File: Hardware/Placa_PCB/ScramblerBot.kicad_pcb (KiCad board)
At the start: 4 copper layers, 79.5 x 70 mm, 74 parts, among them J1 OUT LCD, J10 Conn_01x09_Pin, J2 USB_C_Receptacle_PowerOnly_6P, J3 USB_C_Receptacle_USB2.0_16P, J4 Conn_01x03_Pin, J5 Conn_01x03_Pin, J6 Conn_01x03_Pin, J7 Conn_01x03_Pin, J8 Conn_01x08_Pin, J9 Conn_01x09_Pin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

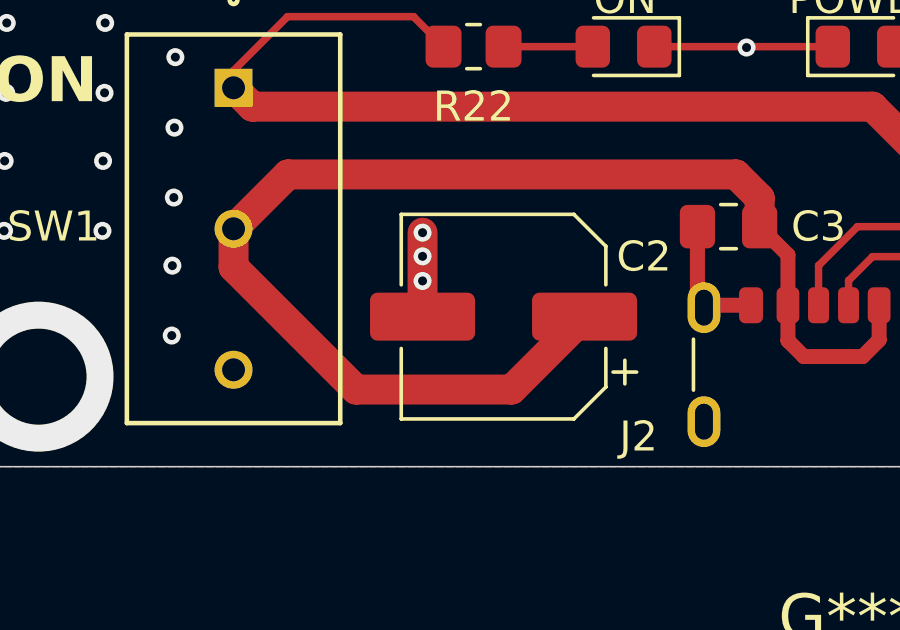
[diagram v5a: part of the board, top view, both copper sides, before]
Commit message: Acomodando capacitor electrolitico de entrada
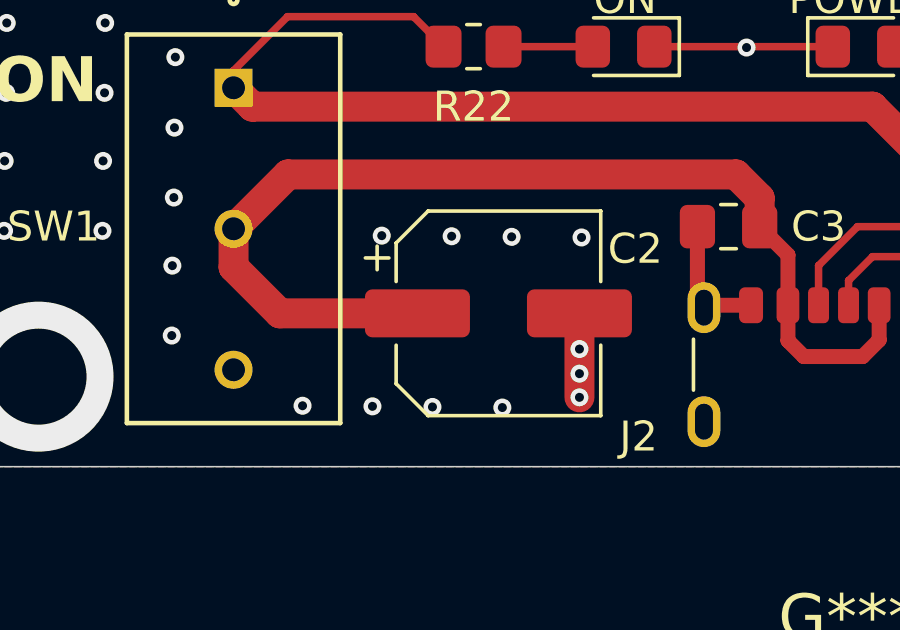
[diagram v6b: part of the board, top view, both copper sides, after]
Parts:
- moved C2 0.20 mm to (126.5, 130.4), turned to 0 degrees
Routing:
- net /Power__USB_C/V_USB_POWER: track 44.1 -> 36.8 mm
- net GNDD: track 129.6 -> 129.3 mm, vias 288 -> 296

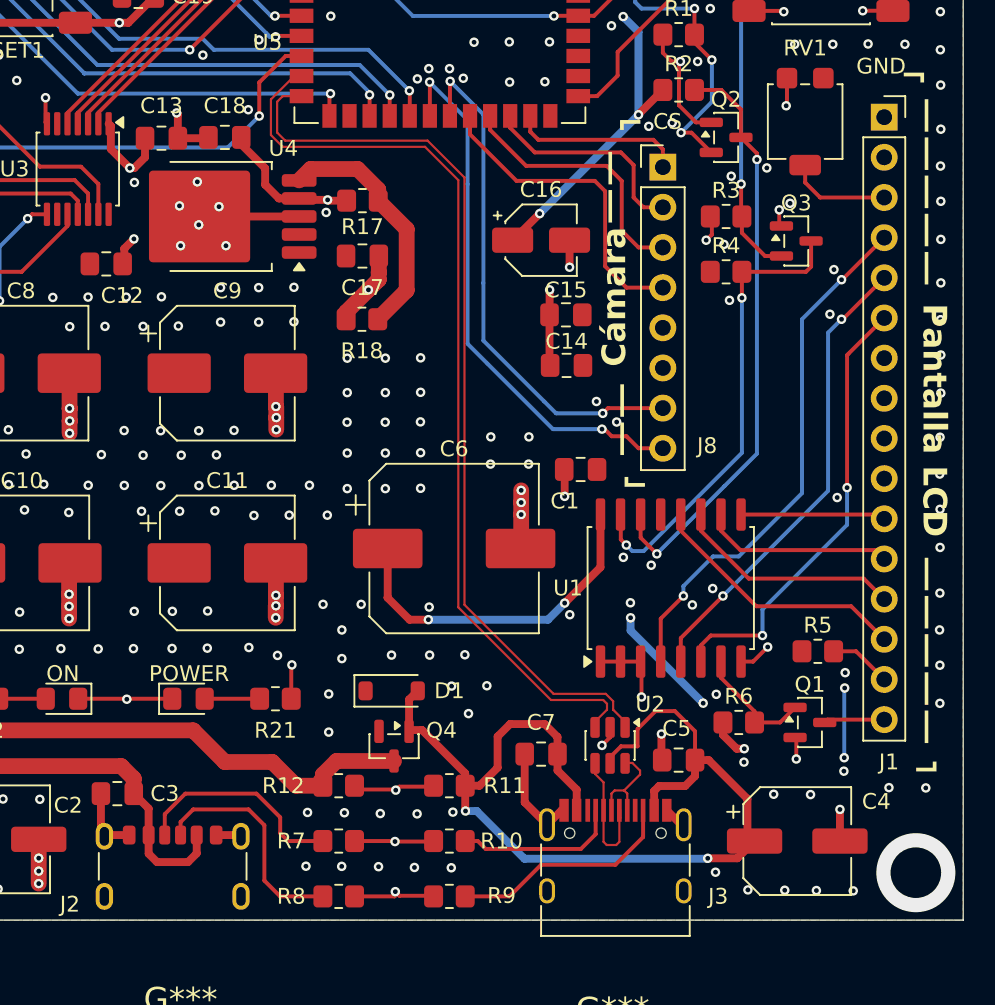
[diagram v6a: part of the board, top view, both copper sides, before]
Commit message: Cambiando algunos errores de DMF y creando Gerbers
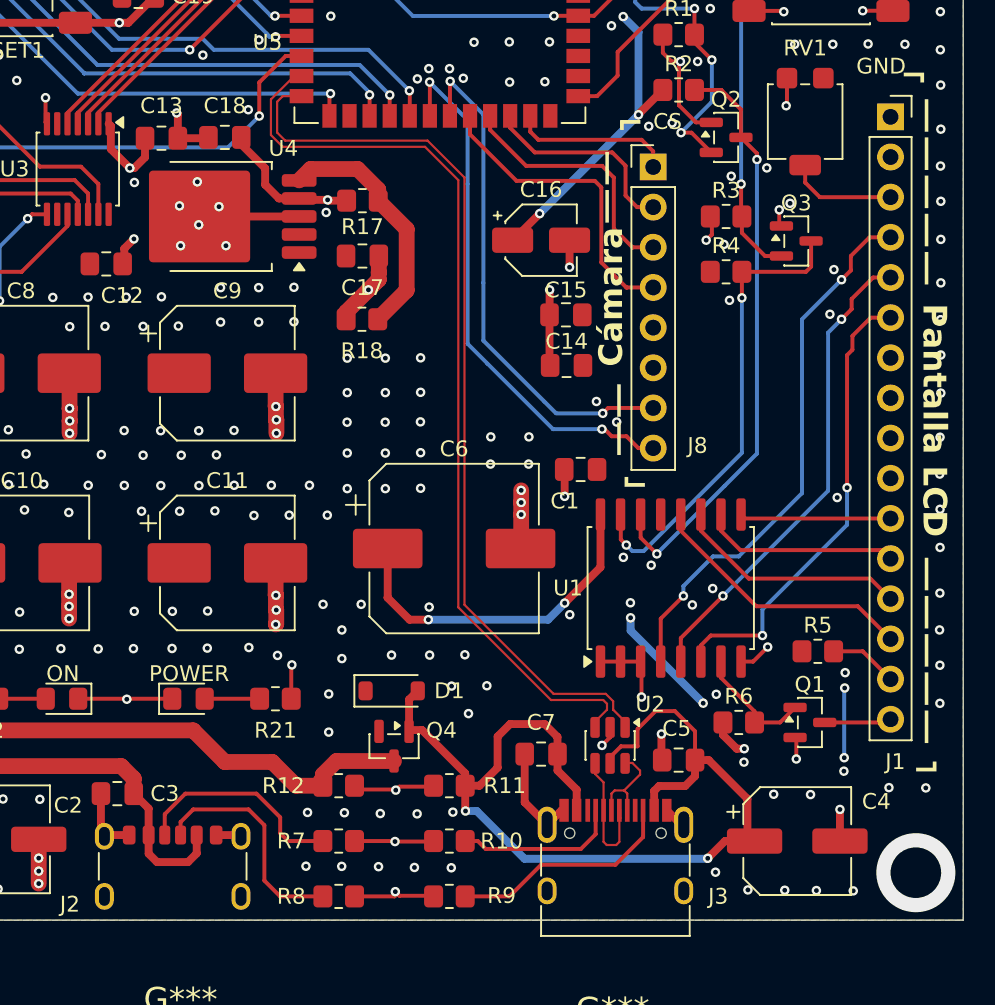
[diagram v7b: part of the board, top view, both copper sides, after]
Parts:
- moved J8 0.61 mm to (168.1, 87.9)
- moved J1 0.40 mm to (183.1, 84.7)
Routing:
- net /Pantalla_LCD/RS: track 33.6 -> 34.6 mm
- net /Pantalla_LCD/EN_LCD: track 28.4 -> 29.4 mm
- net /Pantalla_LCD/RW: track 29.6 -> 30.5 mm
- net /Pantalla_LCD/D4: track 9.17 -> 9.94 mm
- net GNDD: track 129.3 -> 130.0 mm
- net /Camara/MOSI: track 13.7 -> 13.0 mm
- net /Camara/CS: track 11.0 -> 10.3 mm
- net /Camara/SCL: track 34.8 -> 34.2 mm
- net /Camara/SDA: track 32.9 -> 32.3 mm
- net /Camara/SCK: track 20.2 -> 19.6 mm
- net /Camara/MISO: track 16.7 -> 16.2 mm

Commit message: Gerber Final
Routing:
- net /MCU/15: track 37.4 -> 36.8 mm, vias 2 -> 1
- net /MCU/9: track 43.2 -> 42.9 mm, vias 2 -> 1
- net /MCU/17: track 28.6 -> 28.9 mm, vias 2 -> 1
- net /MCU/TX: track 38.4 -> 38.6 mm, vias 2 -> 1
- net /MCU/RX: track 36.8 -> 37.0 mm, vias 2 -> 1
- net /MCU/16: track 26.1 -> 26.0 mm, vias 2 -> 1
- net /MCU/3: vias 2 -> 1
- net /MCU/18: track 32.0 -> 31.9 mm, vias 2 -> 1
- net GNDD: vias 296 -> 194
- net /MCU/10: vias 2 -> 1
- net +5V: vias 39 -> 34
- net +3.3V: vias 17 -> 14
- added copper zone on F.Cu, net GNDD
